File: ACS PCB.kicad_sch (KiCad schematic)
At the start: 4 parts, among them J5 Conn_01x02

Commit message: Finished up PCB [DRAFT]
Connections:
- net Buzzer: now also A1.23 (A9); no longer A1.33 (D33)

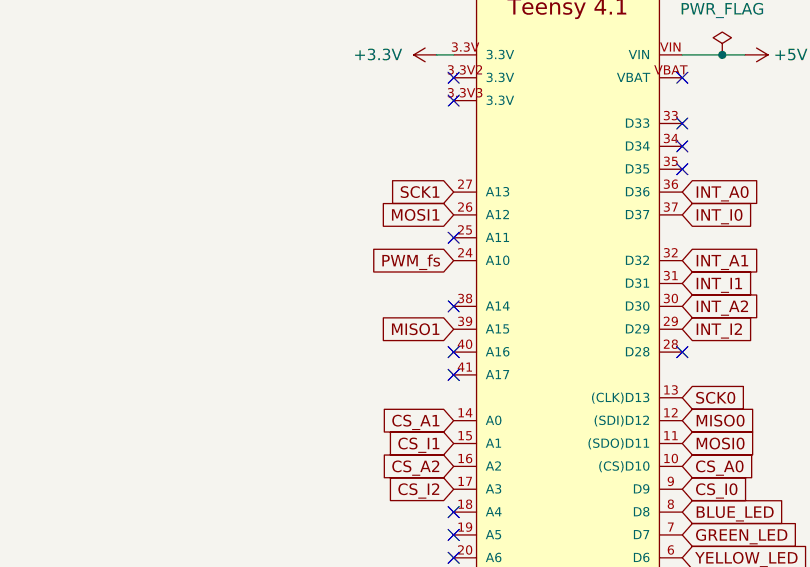
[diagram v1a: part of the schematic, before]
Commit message: Redid Footprints/Picked components
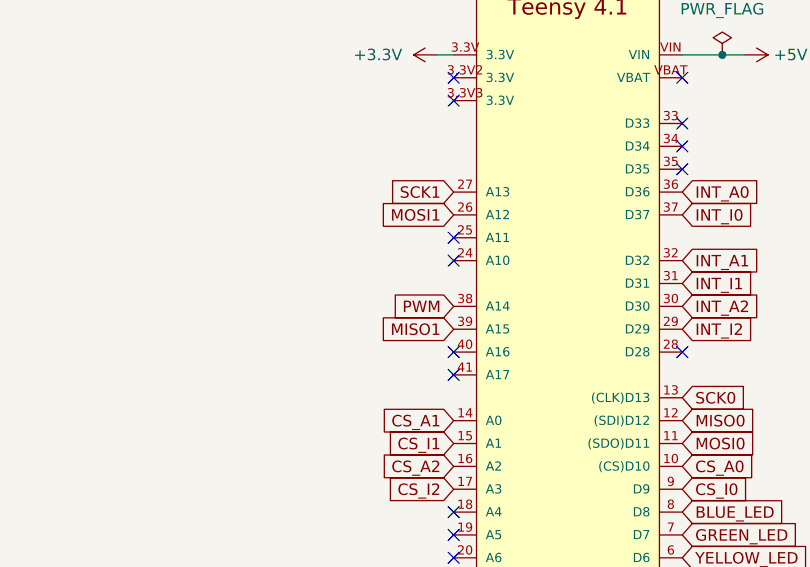
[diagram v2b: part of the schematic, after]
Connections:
- net PWM: now reaches A1.38 (A14)
- net PWM_fs: no longer names the net of A1.24 (A10)
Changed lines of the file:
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@@
-	)
-	(no_connect
-		(at 186.69 60.96)
 	)
 	(no_connect
@@
 	)
 	(no_connect
+		(at 186.69 55.88)
+	)
+	(no_connect
 		(at 212.09 43.18)
 	)
@@
 		)
 	)
-	(global_label "PWM_fs"
-		(shape input)
-		(at 186.69 55.88 180)
+	(global_label "INT_I2"
+		(shape input)
+		(at 212.09 63.5 0)
+		(fields_autoplaced yes)
+		(effects
+			(font
+				(size 1.27 1.27)
+			)
+			(justify left)
+		)
+		(property "Intersheetrefs" "${INTERSHEET_REFS}"
+			(at 220.76 63.5 0)
+			(hide yes)
+			(show_name no)
+			(do_not_autoplace no)
+			(effects
+				(font
+					(size 1.27 1.27)
+				)
+				(justify left)
+			)
+		)
+	)
+	(global_label "INT_A0"
+		(shape input)
+		(at 212.09 48.26 0)
+		(fields_autoplaced yes)
+		(effects
+			(font
+				(size 1.27 1.27)
+			)
+			(justify left)
+		)
+		(property "Intersheetrefs" "${INTERSHEET_REFS}"
+			(at 221.2438 48.26 0)
+			(hide yes)
+			(show_name no)
+			(do_not_autoplace no)
+			(effects
+				(font
+					(size 1.27 1.27)
+				)
+				(justify left)
+			)
+		)
+	)
+	(global_label "BLUE_LED"
+		(shape input)
+		(at 212.09 83.82 0)
+		(fields_autoplaced yes)
+		(effects
+			(font
+				(size 1.27 1.27)
+			)
+			(justify left)
+		)
+		(property "Intersheetrefs" "${INTERSHEET_REFS}"
+			(at 224.2675 83.82 0)
+			(hide yes)
+			(show_name no)
+			(do_not_autoplace no)
+			(effects
+				(font
+					(size 1.27 1.27)
+				)
+				(justify left)
+			)
+		)
+	)
+	(global_label "SCK1"
+		(shape input)
+		(at 186.69 48.26 180)
 		(fields_autoplaced yes)
 		(effects
@@
 		)
 		(property "Intersheetrefs" "${INTERSHEET_REFS}"
-			(at 176.8106 55.88 0)
+			(at 178.7458 48.26 0)
 			(hide yes)
 			(show_name no)
@@
 		)
 	)
-	(global_label "INT_I2"
-		(shape input)
-		(at 212.09 63.5 0)
-		(fields_autoplaced yes)
-		(effects
-			(font
-				(size 1.27 1.27)
-			)
-			(justify left)
-		)
-		(property "Intersheetrefs" "${INTERSHEET_REFS}"
-			(at 220.76 63.5 0)
-			(hide yes)
-			(show_name no)
-			(do_not_autoplace no)
-			(effects
-				(font
-					(size 1.27 1.27)
-				)
-				(justify left)
-			)
-		)
-	)
-	(global_label "INT_A0"
-		(shape input)
-		(at 212.09 48.26 0)
-		(fields_autoplaced yes)
-		(effects
-			(font
-				(size 1.27 1.27)
-			)
-			(justify left)
-		)
-		(property "Intersheetrefs" "${INTERSHEET_REFS}"
-			(at 221.2438 48.26 0)
-			(hide yes)
-			(show_name no)
-			(do_not_autoplace no)
-			(effects
-				(font
-					(size 1.27 1.27)
-				)
-				(justify left)
-			)
-		)
-	)
-	(global_label "BLUE_LED"
-		(shape input)
-		(at 212.09 83.82 0)
-		(fields_autoplaced yes)
-		(effects
-			(font
-				(size 1.27 1.27)
-			)
-			(justify left)
-		)
-		(property "Intersheetrefs" "${INTERSHEET_REFS}"
-			(at 224.2675 83.82 0)
-			(hide yes)
-			(show_name no)
-			(do_not_autoplace no)
-			(effects
-				(font
-					(size 1.27 1.27)
-				)
-				(justify left)
-			)
-		)
-	)
-	(global_label "SCK1"
-		(shape input)
-		(at 186.69 48.26 180)
+	(global_label "INT_A2"
+		(shape input)
+		(at 212.09 60.96 0)
+		(fields_autoplaced yes)
+		(effects
+			(font
+				(size 1.27 1.27)
+			)
+			(justify left)
+		)
+		(property "Intersheetrefs" "${INTERSHEET_REFS}"
+			(at 221.2438 60.96 0)
+			(hide yes)
+			(show_name no)
+			(do_not_autoplace no)
+			(effects
+				(font
+					(size 1.27 1.27)
+				)
+				(justify left)
+			)
+		)
+	)
+	(global_label "INT_A1"
+		(shape input)
+		(at 212.09 55.88 0)
+		(fields_autoplaced yes)
+		(effects
+			(font
+				(size 1.27 1.27)
+			)
+			(justify left)
+		)
+		(property "Intersheetrefs" "${INTERSHEET_REFS}"
+			(at 221.2438 55.88 0)
+			(hide yes)
+			(show_name no)
+			(do_not_autoplace no)
+			(effects
+				(font
+					(size 1.27 1.27)
+				)
+				(justify left)
+			)
+		)
+	)
+	(global_label "RED_LED"
+		(shape input)
+		(at 212.09 91.44 0)
+		(fields_autoplaced yes)
+		(effects
+			(font
+				(size 1.27 1.27)
+			)
+			(justify left)
+		)
+		(property "Intersheetrefs" "${INTERSHEET_REFS}"
+			(at 223.1789 91.44 0)
+			(hide yes)
+			(show_name no)
+			(do_not_autoplace no)
+			(effects
+				(font
+					(size 1.27 1.27)
+				)
+				(justify left)
+			)
+		)
+	)
+	(global_label "PWM"
+		(shape input)
+		(at 186.69 60.96 180)
 		(fields_autoplaced yes)
 		(effects
@@
 		)
 		(property "Intersheetrefs" "${INTERSHEET_REFS}"
-			(at 178.7458 48.26 0)
+			(at 179.532 60.96 0)
 			(hide yes)
 			(show_name no)
@@
 			)
 		)
-	)
-	(global_label "INT_A2"
-		(shape input)
-		(at 212.09 60.96 0)
-		(fields_autoplaced yes)
-		(effects
-			(font
-				(size 1.27 1.27)
-			)
-			(justify left)
-		)
-		(property "Intersheetrefs" "${INTERSHEET_REFS}"
-			(at 221.2438 60.96 0)
-			(hide yes)
-			(show_name no)
-			(do_not_autoplace no)
-			(effects
-				(font
-					(size 1.27 1.27)
-				)
-				(justify left)
-			)
-		)
-	)
-	(global_label "INT_A1"
-		(shape input)
-		(at 212.09 55.88 0)
-		(fields_autoplaced yes)
-		(effects
-			(font
-				(size 1.27 1.27)
-			)
-			(justify left)
-		)
-		(property "Intersheetrefs" "${INTERSHEET_REFS}"
-			(at 221.2438 55.88 0)
-			(hide yes)
-			(show_name no)
-			(do_not_autoplace no)
-			(effects
-				(font
-					(size 1.27 1.27)
-				)
-				(justify left)
-			)
-		)
-	)
-	(global_label "RED_LED"
-		(shape input)
-		(at 212.09 91.44 0)
-		(fields_autoplaced yes)
-		(effects
-			(font
-				(size 1.27 1.27)
-			)
-			(justify left)
-		)
-		(property "Intersheetrefs" "${INTERSHEET_REFS}"
-			(at 223.1789 91.44 0)
-			(hide yes)
-			(show_name no)
-			(do_not_autoplace no)
-			(effects
-				(font
-					(size 1.27 1.27)
-				)
-				(justify left)
-			)
-		)

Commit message: finalized
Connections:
- net +BATT: now also F1.2; no longer F1.1
- net GND: now also J5.1 (Pin_1); no longer J5.2 (Pin_2)
- new net: F1.1, J5.2 (Pin_2)
